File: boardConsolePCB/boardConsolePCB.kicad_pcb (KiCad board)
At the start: 2 copper layers, 141 x 90 mm, 132 parts, among them J1 to HV cable, J2 SMA F, J3 PROG, J4 BUTTONS, J5 PWR, J6 FUEL/TRIM, J7 PRG_UART, Q1 BC548, Q2 IRML0030TR, Q3 IRML0030TR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

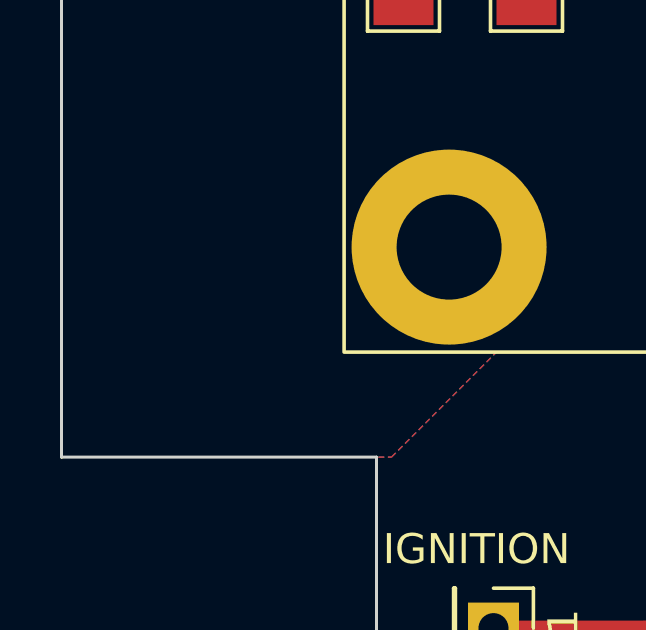
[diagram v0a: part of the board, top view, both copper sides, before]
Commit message: added manu map
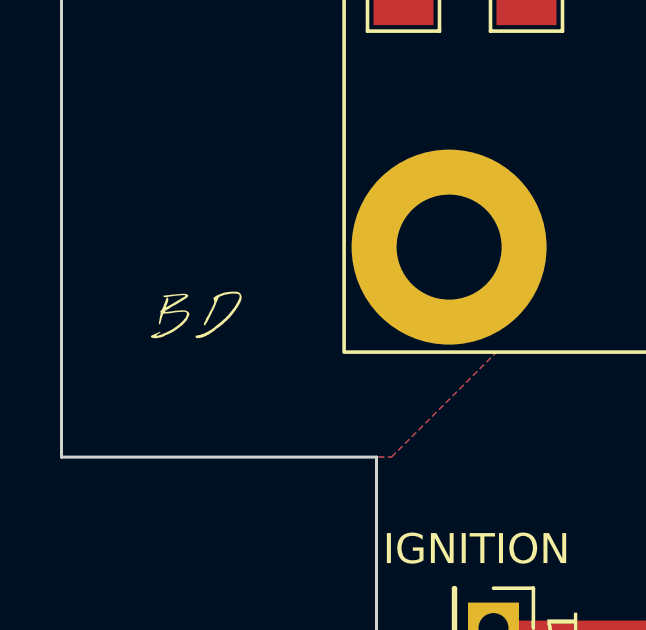
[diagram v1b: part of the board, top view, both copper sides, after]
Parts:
- added G***: LOGO, BartLib_Logo:BD_small 3.5x2.6, F.Cu at (92.0, 123.8)
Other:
- board text added: "Board Console PCB design Copyright (C) 2023 Bartosz Pracz This PCB design is free hardware: you can redistribute it and/or modify it under the terms of the GNU General Public License as published by the Free Software Foundation, either version 3 of the License, or (at your option) any later version. This PCS design is distributed in the hope that it will be useful, but WITHOUT ANY WARRANTY; witho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"
- board text removed: "Board Console PCB design Copyright (C) 2023 Bartosz Pracz This program is free software: you can redistribute it and/or modify it under the terms of the GNU General Public License as published by the Free Software Foundation, either version 3 of the License, or (at your option) any later version. This program is distributed in the hope that it will be useful, but WITHOUT ANY WARRANTY; without eve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"

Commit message: add GDT
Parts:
- added GD1: CG90L, boardConsoleLib:CG90L, F.Cu at (134.2, 140.7)
- C10, C28: value 0m1 -> 1000u 10V
- C31: value 1000uF -> 1000uF 25V
- R20: value 1k -> 1k (NM)
- moved D2 0.70 mm to (134.4, 133.5)
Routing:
- net Net-(D2-K): track 5.96 -> 11.9 mm
